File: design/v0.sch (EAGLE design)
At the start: 30 parts, among them U1 CHERRY-MX, U2 CHERRY-MX, U3 CHERRY-MX, U4 CHERRY-MX, U5 CHERRY-MX, U6 CHERRY-MX, U7 CHERRY-MX, U8 CHERRY-MX, U9 CHERRY-MX

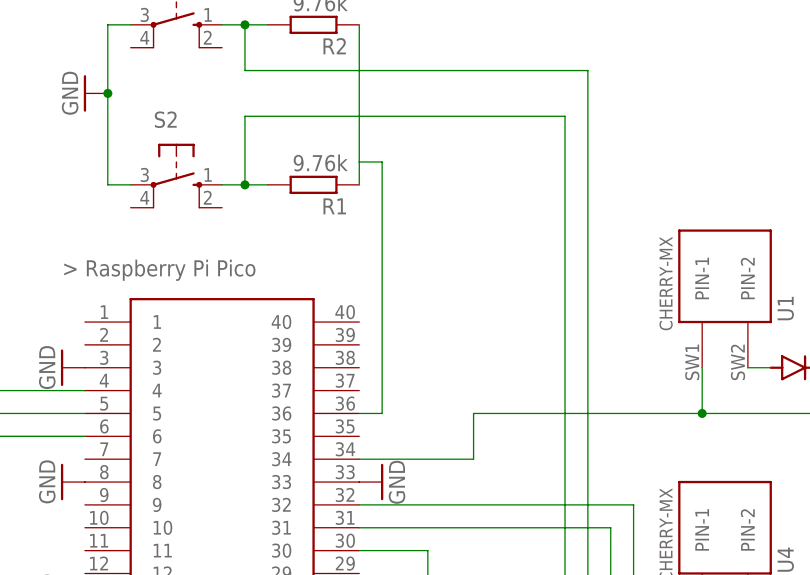
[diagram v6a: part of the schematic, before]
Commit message: Add missing ground marker
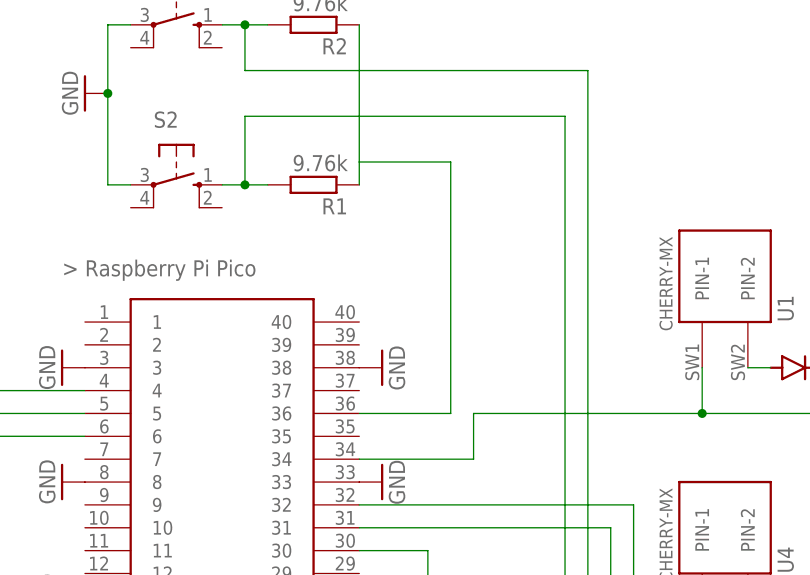
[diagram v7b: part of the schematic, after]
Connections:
- net GND: now also U$1.38
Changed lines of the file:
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@@
 <part name="R2" library="rcl" library_urn="urn:adsk.eagle:library:334" deviceset="R-EU_" device="VMTA55" package3d_urn="urn:adsk.eagle:package:26121/2" value="9.76k"/>
 <part name="GND13" library="supply1" library_urn="urn:adsk.eagle:library:371" deviceset="GND" device=""/>
+<part name="GND12" library="supply1" library_urn="urn:adsk.eagle:library:371" deviceset="GND" device=""/>
 </parts>
 <sheets>
@@
 <instance part="GND13" gate="1" x="66.04" y="93.98" smashed="yes" rot="R270">
 <attribute name="VALUE" x="63.5" y="96.52" size="1.778" layer="96" rot="R270"/>
+</instance>
+<instance part="GND12" gate="1" x="99.06" y="63.5" smashed="yes" rot="R90">
+<attribute name="VALUE" x="101.6" y="60.96" size="1.778" layer="96" rot="R90"/>
 </instance>
 </instances>
@@
 <junction x="68.58" y="93.98"/>
 </segment>
+<segment>
+<pinref part="U$1" gate="G$1" pin="38"/>
+<pinref part="GND12" gate="1" pin="GND"/>
+</segment>
 </net>
 <net name="N$4" class="0">
@@
 <wire x1="96.52" y1="101.6" x2="96.52" y2="86.36" width="0.1524" layer="91"/>
 <wire x1="96.52" y1="86.36" x2="96.52" y2="83.82" width="0.1524" layer="91"/>
-<wire x1="96.52" y1="86.36" x2="99.06" y2="86.36" width="0.1524" layer="91"/>
+<wire x1="96.52" y1="86.36" x2="106.68" y2="86.36" width="0.1524" layer="91"/>
 <pinref part="U$1" gate="G$1" pin="36"/>
-<wire x1="99.06" y1="58.42" x2="96.52" y2="58.42" width="0.1524" layer="91"/>
-<wire x1="99.06" y1="86.36" x2="99.06" y2="58.42" width="0.1524" layer="91"/>
-</segment>
-</net>
+<wire x1="106.68" y1="58.42" x2="96.52" y2="58.42" width="0.1524" layer="91"/>
+<wire x1="106.68" y1="86.36" x2="106.68" y2="58.42" width="0.1524" layer="91"/>
+</segment>
+</net>
